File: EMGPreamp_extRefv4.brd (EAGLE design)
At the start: 23.2 x 34.9 mm, 25 parts, among them U1 TLE2426CD

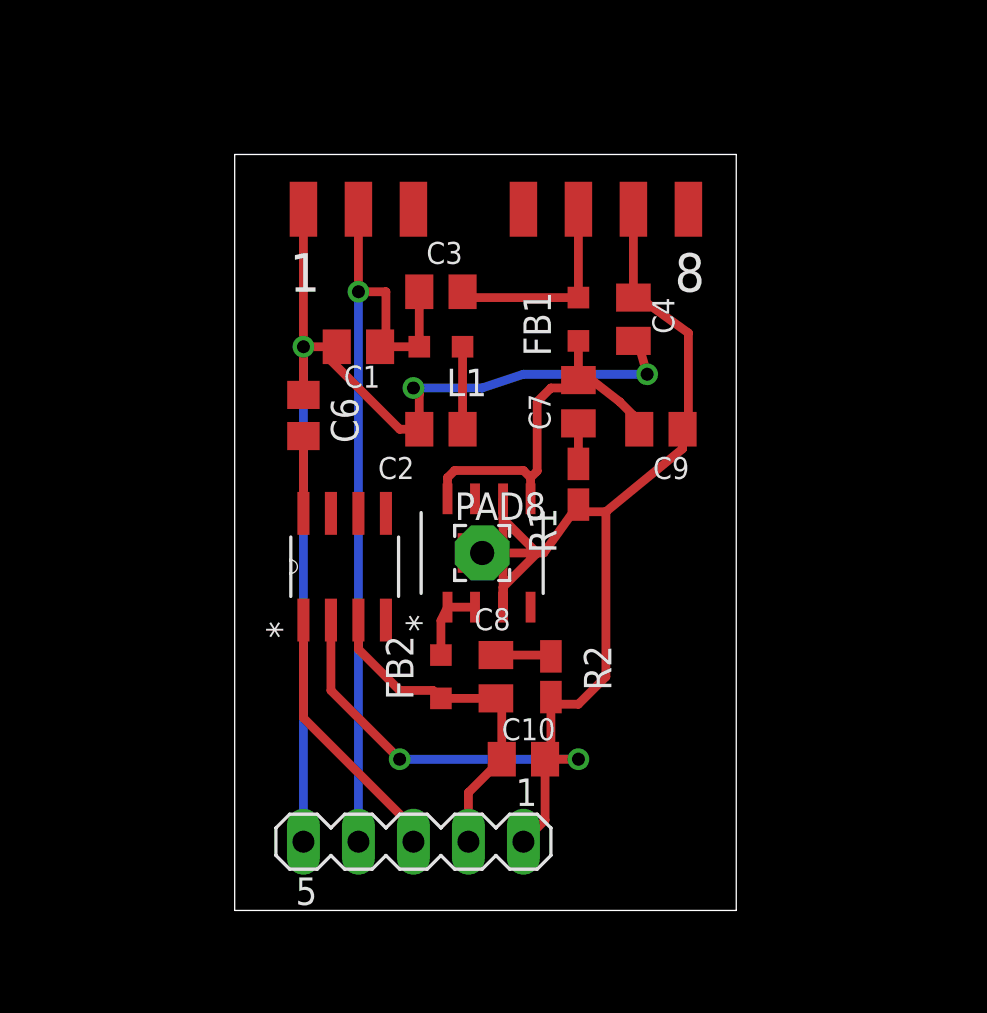
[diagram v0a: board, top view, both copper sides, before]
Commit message: new preamp board with capacitive input coupling
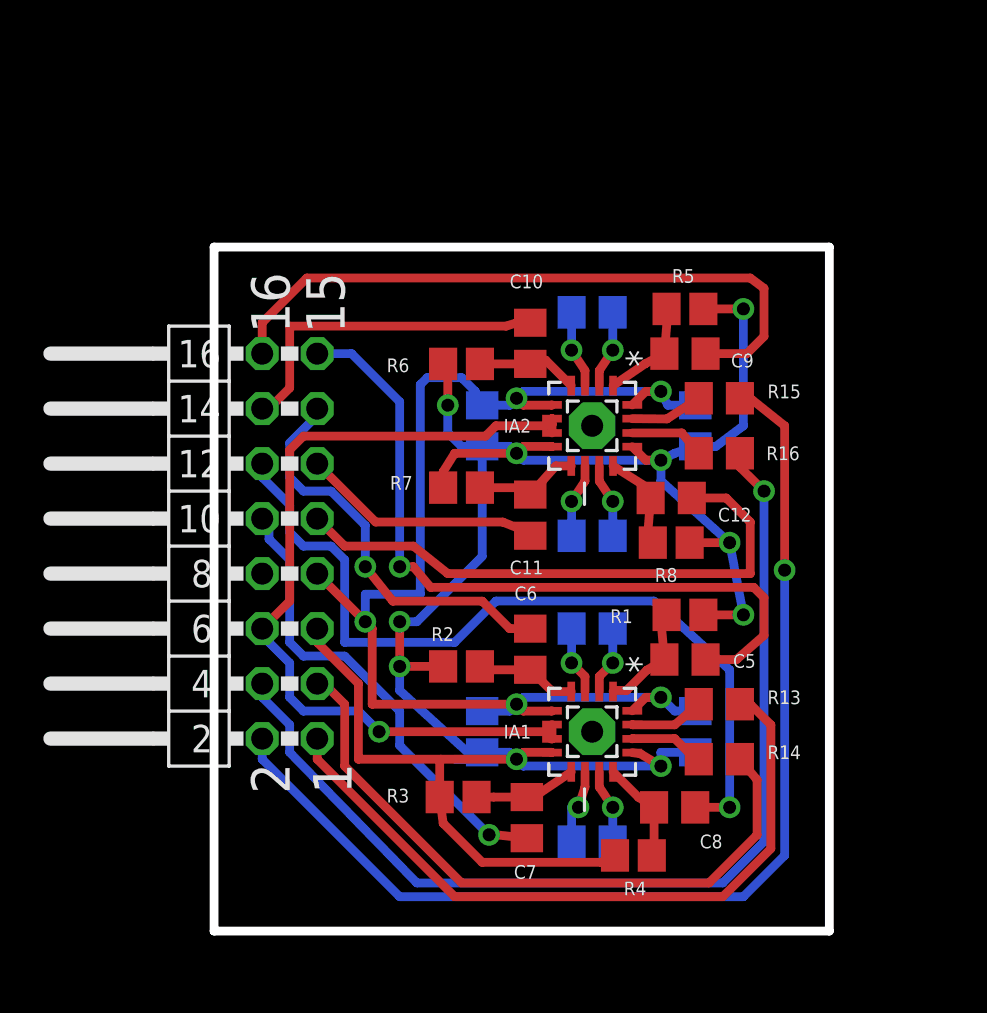
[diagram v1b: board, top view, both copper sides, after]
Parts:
- removed FB1, FB2: (no value), rcl:L2012C
- removed L1: 12uH, resistor:L2012C
- removed PAD3, PAD4, PAD5, PAD6, PAD7: (no value), wirepad:SMD1,27-2,54
- removed PAD8: (no value), wirepad:2,54/1,1
- removed U$1: ADP7105-REGULATOR, tuckerLib:ADP7105-REGULATOR
- removed U1: TLE2426CD, Texas Instruments_By_element14_Batch_1:SOIC127P600X175-8N
- added C11, C12, C5: 22uF, rcl:C0805
- added IA1, IA2: AD8224HBCPZ-R7, Analog Devices_By_element14_Batch1:QFN65P400X400X100-16N
- added R10, R11, R12, R9: 499, rcl:R0805
- added R13, R14, R15, R16: 49.9, rcl:R0805
- added R3, R4, R5, R6, R7, R8: 1.8k, resistor:R0805
- C1, C2: value 10uf -> 0.1uF; device rcl:C0805K -> rcl:C0805
- C10, C9: value 2uf -> 22uF; device rcl:C0805K -> rcl:C0805
- C3, C4: value 470pf -> 0.1uF; device rcl:C0805K -> rcl:C0805
- C6: value 1uF -> 22uF
- C7, C8: value 22uf -> 22uF; device rcl:C0805K -> rcl:C0805
- PAD1, PAD2: value (none) -> WIREPAD2,15/1,0; device wirepad:SMD1,27-2,54 -> wirepad:2,15/1,0
- R1, R2: value 0.91 -> 1.8k; device resistor:R2012W -> resistor:R0805
- SV1: device con-lstb:MA05-1 -> con-lstb:MA08-2W
- moved PAD2 26.4 mm to (16.5, 8.26), turned to 180 degrees
- moved C7 19.4 mm to (13.5, 4.29), turned to 90 degrees
- moved C10 19.2 mm to (13.7, 26.2), turned to 270 degrees
- moved C1 18.7 mm to (11.4, 8.26), flipped to the bottom, turned to 270 degrees
- moved C2 18.3 mm to (21.3, 8.26), flipped to the bottom, turned to 270 degrees
- moved PAD1 16.7 mm to (16.5, 22.4), turned to 180 degrees
- moved C6 15.0 mm to (13.7, 12.1), turned to 270 degrees
- moved SV1 14.8 mm to (2.54, 16.8), turned to 90 degrees
- moved C8 10.2 mm to (20.3, 4.76), turned to 180 degrees
- moved R1 7.79 mm to (20.8, 13.7), turned to 180 degrees
- moved C3 6.48 mm to (11.4, 22.4), flipped to the bottom, turned to 270 degrees
- moved C4 5.69 mm to (21.3, 22.4), flipped to the bottom
- moved R2 4.15 mm to (10.5, 11.3), turned to 0 degrees
- moved C9 3.67 mm to (20.8, 25.7), turned to 180 degrees
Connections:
- removed net N$1: C2.1, L1.2
- removed net N$2: C6.1, U1.8
- removed net N$3: C8.2, R2.2
- removed net N$4: C7.2, R1.2
- removed net NC0: PAD3.1
- removed net NC1: PAD4.1
- removed net NC2: PAD7.1
- removed net NC3: U$1.4
- removed net PG: U$1.7
- removed net VS1+: C3.1, FB1.1, PAD5.1
- removed net VS1-: C10.2, C4.1, C9.2, PAD6.1, PAD8.1, R1.1, R2.1, SV1.1, U$1.3, U$1.6, U$1.9, U1.2
- removed net VS1F+: C7.1, C9.1, FB1.2, U$1.5, U$1.8
- removed net VS2+: FB2.1, U$1.1, U$1.2
- removed net VS2F+: C10.1, C8.1, FB2.2, SV1.2, U1.3
- new net I11: C5.2, IA1.1, R1.2
- new net I12: C6.2, IA1.4, R2.2
- new net I13: C7.2, IA1.9, R3.2
- new net I14: C8.2, IA1.12, R4.2
- new net I21: C9.2, IA2.1, R5.2
- new net I22: C10.2, IA2.4, R6.2
- new net I23: C11.2, IA2.9, R7.2
- new net I24: C12.2, IA2.12, R8.2
- new net IN1+: C6.1, SV1.13
- new net IN1-: C5.1, SV1.15
- new net IN2+: C7.1, SV1.10
- new net IN2-: C8.1, SV1.12
- new net IN3+: C10.1, SV1.14
- new net IN3-: C9.1, SV1.16
- new net IN4+: C11.1, SV1.11
- new net IN4-: C12.1, SV1.9
- new net O1: IA1.15, R13.1
- new net O2: IA1.14, R14.1
- new net O3: IA2.15, R15.1
- new net O4: IA2.14, R16.1
- new net OUT1: R13.2, SV1.1
- new net OUT2: R14.2, SV1.3
- new net OUT3: R15.2, SV1.2
- new net OUT4: R16.2, SV1.4
- new net RG1: IA1.3, R9.1
- new net RG1_2: IA1.2, R9.2
- new net RG2: IA1.11, R10.1
- new net RG2_2: IA1.10, R10.2
- new net RG3: IA2.3, R11.1
- new net RG3_2: IA2.2, R11.2
- new net RG4: IA2.11, R12.1
- new net RG4_2: IA2.10, R12.2
- net GND: now also C3.2, IA1.13, IA1.8, IA2.13, IA2.8, R1.1, R2.1, R3.1, R4.1, R5.1, R6.1, R7.1, R8.1; no longer C6.2, PAD1.1
- net VCC: now also C2.1, C3.1, C4.1, IA1.16, IA1.5, IA2.16, IA2.5, SV1.7; no longer C3.2, L1.1, PAD2.1, SV1.4
- net VREF: now also IA1.6, IA1.7, IA2.6, IA2.7, SV1.6; no longer SV1.3, U1.1
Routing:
- net VS1-: track 72.4 -> 0.00 mm, vias 2 -> 0
- net GND: track 53.7 -> 107.1 mm, vias 3 -> 10
- net OUT3: track 0.00 -> 50.9 mm, vias 0 -> 1
- net OUT4: track 0.00 -> 47.3 mm, vias 0 -> 1
- net IN2-: track 0.00 -> 38.6 mm, vias 0 -> 1
- net IN1-: track 0.00 -> 34.7 mm, vias 0 -> 1
- net OUT1: track 0.00 -> 33.0 mm
- net IN3-: track 0.00 -> 30.9 mm
- net OUT2: track 0.00 -> 30.5 mm
- net VREF: track 12.3 -> 39.9 mm, vias 0 -> 1
- net IN4-: track 0.00 -> 26.8 mm
- net IN2+: track 0.00 -> 21.8 mm, vias 0 -> 1
- net VCC: track 37.6 -> 58.5 mm, vias 1 -> 5
- net IN1+: track 0.00 -> 19.5 mm, vias 0 -> 1
- net VS1F+: track 17.9 -> 0.00 mm
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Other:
- board size 23.2 x 34.9 mm -> 28.4 x 31.6 mm
- board text added: "15"
- board text added: "16"
- board text added: "2"
- board text added: "4CH preamp"
- board text added: "V4 rev1"
- board text removed: "2.5V@300mA"
- board text removed: "5V@300mA"
- board text removed: "8"
- board text removed: "DC-DC isolator"
- board text removed: "V1"
- board text removed: "and voltage"
- board text removed: "input 9-18V@1A"
- board text removed: "output:"
- board text removed: "regulator"

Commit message: routing improvements- attempting to isolate inputs from outputs better
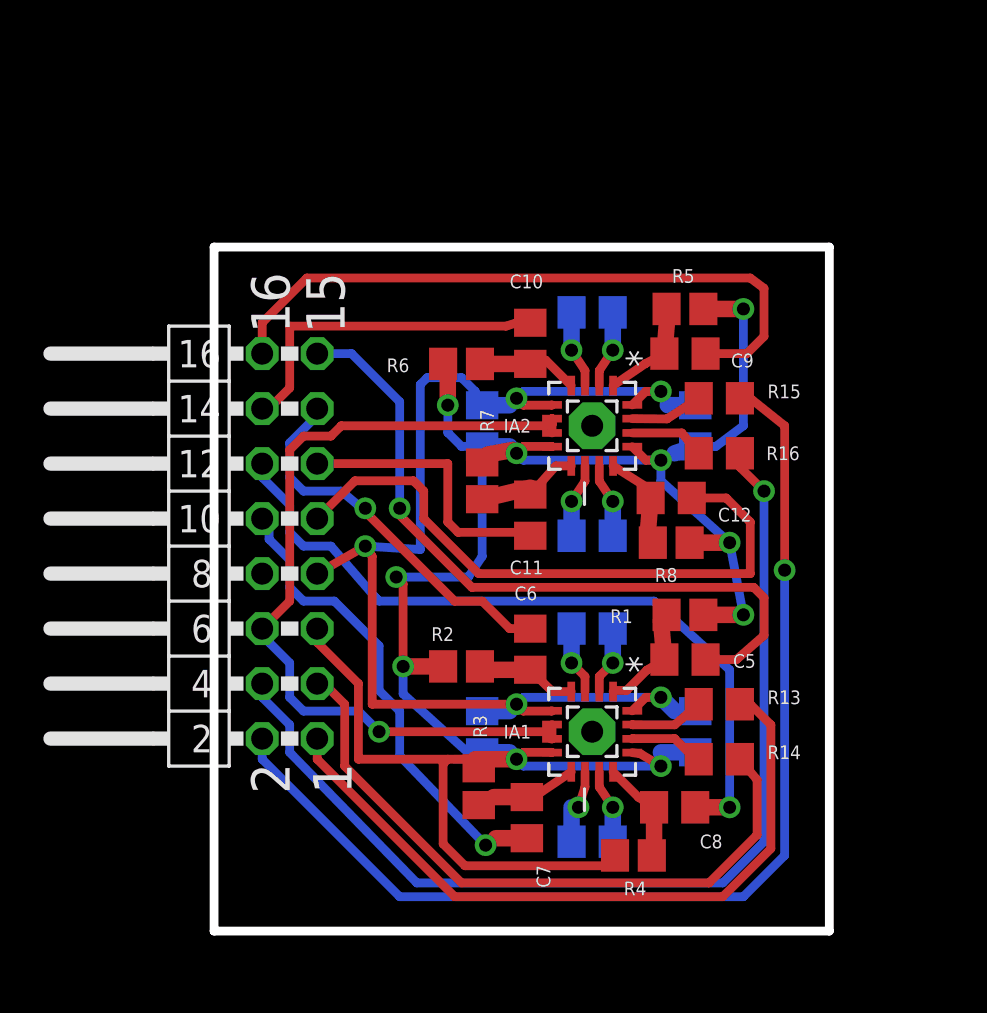
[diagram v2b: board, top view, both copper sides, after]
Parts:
- moved R3 1.06 mm to (11.3, 5.71), turned to 270 degrees
- moved R7 1.00 mm to (11.4, 19.8), turned to 270 degrees
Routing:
- net IN2-: track 38.6 -> 34.9 mm
- net IN4+: track 11.8 -> 14.1 mm
- net IN4-: track 26.8 -> 29.1 mm
- net IN1-: track 34.7 -> 33.2 mm
- net IN1+: track 19.5 -> 18.4 mm

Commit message: updated power board designs: v2 uses low current 2.5v reference, v3 uses 10v rail and 5v ref both with simple linear regulators. Added breakout board to go from DB37 to BNC
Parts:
- C10, C11, C12, C5, C6, C7, C8, C9: value 22uF -> 4700pF
- R1, R2, R3, R4, R5, R6, R7, R8: value 1.8k -> 1M
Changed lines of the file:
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@@
 <attribute name="NAME" x="17.145" y="15.39875" size="0.635" layer="26" rot="MR0"/>
 </element>
-<element name="C5" library="rcl" package="C0805" value="22uF" x="20.79625" y="11.58875" smashed="yes" rot="R180">
+<element name="C5" library="rcl" package="C0805" value="4700pF" x="20.79625" y="11.58875" smashed="yes" rot="R180">
 <attribute name="NAME" x="24.06424375" y="11.84049375" size="0.635" layer="25" rot="R180"/>
 </element>
-<element name="C6" library="rcl" package="C0805" value="22uF" x="13.6525" y="12.065" smashed="yes" rot="R270">
+<element name="C6" library="rcl" package="C0805" value="4700pF" x="13.6525" y="12.065" smashed="yes" rot="R270">
 <attribute name="NAME" x="12.924503125" y="14.32601875" size="0.635" layer="25"/>
 </element>
-<element name="C7" library="rcl" package="C0805" value="22uF" x="13.49375" y="4.28625" smashed="yes" rot="R90">
+<element name="C7" library="rcl" package="C0805" value="4700pF" x="13.49375" y="4.28625" smashed="yes" rot="R90">
 <attribute name="NAME" x="13.942759375" y="2.0956625" size="0.635" layer="25" rot="R270"/>
 </element>
-<element name="C8" library="rcl" package="C0805" value="22uF" x="20.32" y="4.7625" smashed="yes" rot="R180">
+<element name="C8" library="rcl" package="C0805" value="4700pF" x="20.32" y="4.7625" smashed="yes" rot="R180">
 <attribute name="NAME" x="22.526546875" y="3.5037875" size="0.635" layer="25" rot="R180"/>
 </element>
-<element name="C9" library="rcl" package="C0805" value="22uF" x="20.79625" y="25.7175" smashed="yes" rot="R180">
+<element name="C9" library="rcl" package="C0805" value="4700pF" x="20.79625" y="25.7175" smashed="yes" rot="R180">
 <attribute name="NAME" x="23.97125" y="25.7175" size="0.635" layer="25" rot="R180"/>
 </element>
-<element name="C10" library="rcl" package="C0805" value="22uF" x="13.6525" y="26.19375" smashed="yes" rot="R270">
+<element name="C10" library="rcl" package="C0805" value="4700pF" x="13.6525" y="26.19375" smashed="yes" rot="R270">
 <attribute name="NAME" x="12.70000625" y="28.73375" size="0.635" layer="25"/>
 </element>
-<element name="C11" library="rcl" package="C0805" value="22uF" x="13.6525" y="18.25625" smashed="yes" rot="R90">
+<element name="C11" library="rcl" package="C0805" value="4700pF" x="13.6525" y="18.25625" smashed="yes" rot="R90">
 <attribute name="NAME" x="14.248975" y="16.15865625" size="0.635" layer="25" rot="R180"/>
 </element>
-<element name="C12" library="rcl" package="C0805" value="22uF" x="20.16125" y="19.05" smashed="yes" rot="R180">
+<element name="C12" library="rcl" package="C0805" value="4700pF" x="20.16125" y="19.05" smashed="yes" rot="R180">
 <attribute name="NAME" x="23.866978125" y="18.59631875" size="0.635" layer="25" rot="R180"/>
 </element>
@@
 <attribute name="VALUE" x="6.35" y="14.2875" size="1.27" layer="27" ratio="10" rot="R90"/>
 </element>
-<element name="R1" library="resistor" package="R0805" value="1.8k" x="20.79625" y="13.6525" smashed="yes" rot="R180">
+<element name="R1" library="resistor" package="R0805" value="1M" x="20.79625" y="13.6525" smashed="yes" rot="R180">
 <attribute name="NAME" x="18.38325" y="13.9065" size="0.635" layer="25" rot="R180"/>
 </element>
-<element name="R2" library="resistor" package="R0805" value="1.8k" x="10.4775" y="11.27125" smashed="yes">
+<element name="R2" library="resistor" package="R0805" value="1M" x="10.4775" y="11.27125" smashed="yes">
 <attribute name="NAME" x="9.0805" y="12.446" size="0.635" layer="25"/>
 </element>
-<element name="R3" library="resistor" package="R0805" value="1.8k" x="11.27125" y="5.715" smashed="yes" rot="R270">
+<element name="R3" library="resistor" package="R0805" value="1M" x="11.27125" y="5.715" smashed="yes" rot="R270">
 <attribute name="NAME" x="11.01725" y="9.017" size="0.635" layer="25" rot="R270"/>
 </element>
-<element name="R4" library="resistor" package="R0805" value="1.8k" x="18.415" y="2.54" smashed="yes">
+<element name="R4" library="resistor" package="R0805" value="1M" x="18.415" y="2.54" smashed="yes">
 <attribute name="NAME" x="17.9705" y="0.6985" size="0.635" layer="25"/>
 </element>
-<element name="R5" library="resistor" package="R0805" value="1.8k" x="20.79625" y="27.78125" smashed="yes" rot="R180">
+<element name="R5" library="resistor" package="R0805" value="1M" x="20.79625" y="27.78125" smashed="yes" rot="R180">
 <attribute name="NAME" x="21.24075" y="29.62275" size="0.635" layer="25" rot="R180"/>
 </element>
-<element name="R6" library="resistor" package="R0805" value="1.8k" x="10.4775" y="25.24125" smashed="yes">
+<element name="R6" library="resistor" package="R0805" value="1M" x="10.4775" y="25.24125" smashed="yes">
 <attribute name="NAME" x="8.0645" y="25.49525" size="0.635" layer="25" rot="R180"/>
 </element>
-<element name="R7" library="resistor" package="R0805" value="1.8k" x="11.43" y="19.84375" smashed="yes" rot="R270">
+<element name="R7" library="resistor" package="R0805" value="1M" x="11.43" y="19.84375" smashed="yes" rot="R270">
 <attribute name="NAME" x="11.33475" y="23.14575" size="0.635" layer="25" rot="R270"/>
 </element>
-<element name="R8" library="resistor" package="R0805" value="1.8k" x="20.16125" y="16.98625" smashed="yes" rot="R180">
+<element name="R8" library="resistor" package="R0805" value="1M" x="20.16125" y="16.98625" smashed="yes" rot="R180">
 <attribute name="NAME" x="20.447" y="15.8115" size="0.635" layer="25" rot="R180"/>
 </element>
